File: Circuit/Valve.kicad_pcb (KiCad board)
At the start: 2 copper layers, 96.5 x 63.5 mm, 20 parts, among them CN1 GROVE, CN2 ST-LINK, CN3 TTL-232R-3V3, J1 Conn_01x02_Male, SW1 RESET, U1 STM32L010F4P6

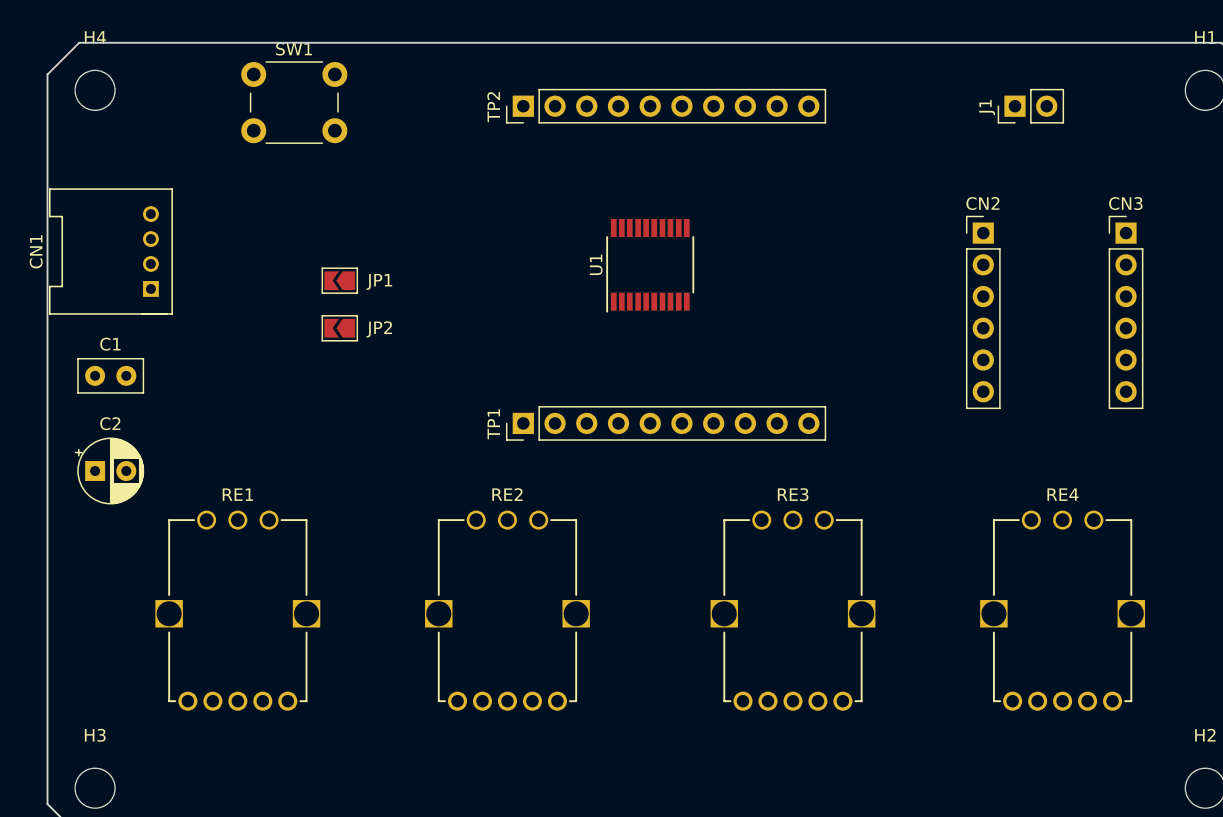
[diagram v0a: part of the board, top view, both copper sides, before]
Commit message: 回路図を修正
* 電源コネクタ (2P) を I2C 兼用 4P に変更
* I2C ADDR パッドを削除して LED と抵抗に置換
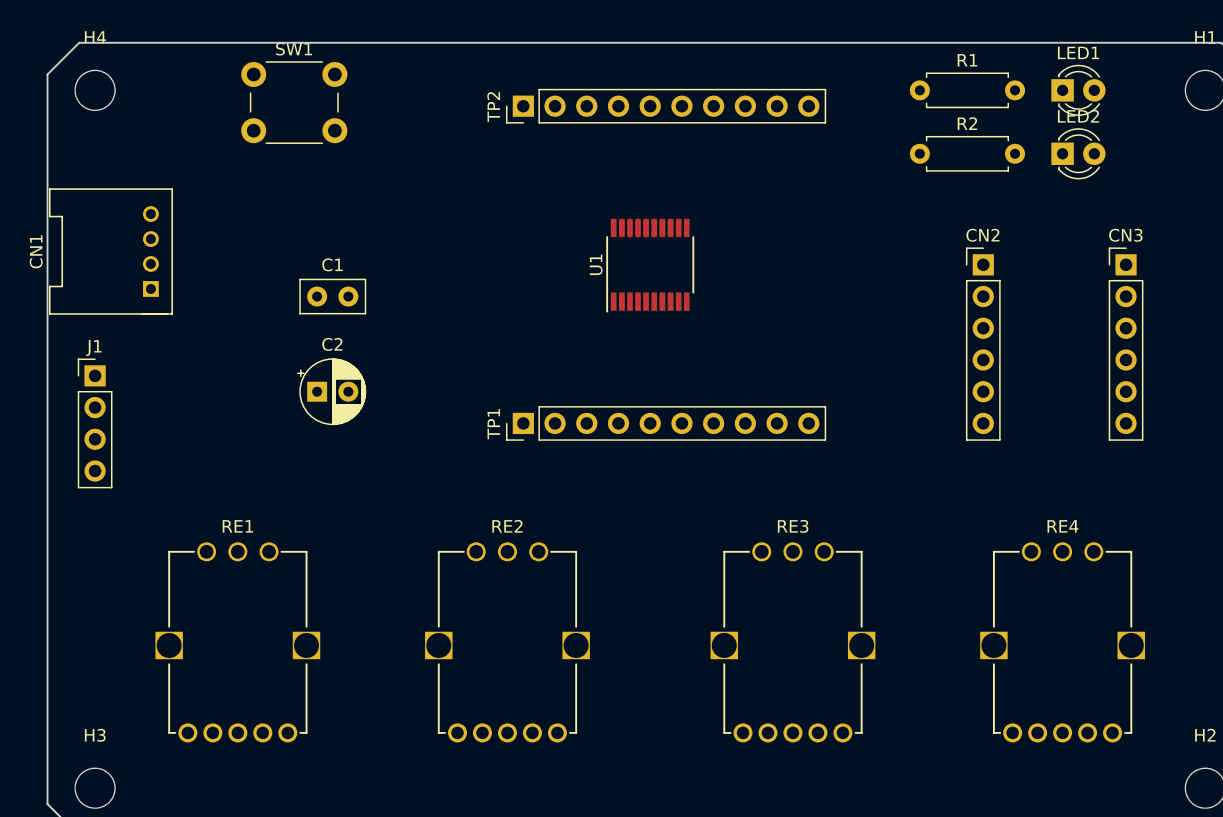
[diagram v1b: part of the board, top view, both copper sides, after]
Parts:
- removed JP1: I2C_ADDR_A0, Jumper:SolderJumper-2_P1.3mm_Open_TrianglePad1.0x1.5mm
- removed JP2: I2C_ADDR_A1, Jumper:SolderJumper-2_P1.3mm_Open_TrianglePad1.0x1.5mm
- added LED1: LED, LED_THT:LED_D3.0mm, F.Cu at (154.9, 52.1)
- added LED2: LED, LED_THT:LED_D3.0mm, F.Cu at (154.9, 57.1)
- added R1: 1k, Resistor_THT:R_Axial_DIN0207_L6.3mm_D2.5mm_P7.62mm_Horizontal, F.Cu at (143.5, 52.1)
- added R2: 1k, Resistor_THT:R_Axial_DIN0207_L6.3mm_D2.5mm_P7.62mm_Horizontal, F.Cu at (143.5, 57.1)
- J1: value Conn_01x02_Male -> Conn_01x04_Male; footprint Connector_PinHeader_2.54mm:PinHeader_1x02_P2.54mm_Vertical -> Connector_PinHeader_2.54mm:PinHeader_1x04_P2.54mm_Vertical
- moved J1 76.8 mm to (77.5, 74.9), turned to 0 degrees
- moved C1 18.9 mm to (95.2, 68.6)
- moved C2 18.9 mm to (95.2, 76.2)
- moved CN2 2.54 mm to (148.6, 66.0)
- moved CN3 2.54 mm to (160.0, 66.0)
- moved RE1 2.54 mm to (88.9, 96.5)
- moved RE2 2.54 mm to (110.5, 96.5)
- moved RE3 2.54 mm to (133.3, 96.5)
- moved RE4 2.54 mm to (154.9, 96.5)
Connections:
- J1 pad 1: VDD -> GND
- J1 pad 2: GND -> VDD
